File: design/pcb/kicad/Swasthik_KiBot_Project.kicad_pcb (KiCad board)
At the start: 2 copper layers, 30.4 x 14.7 mm, 5 parts, among them J1 Screw_Terminal_01x02, J2 Screw_Terminal_01x02, U1 NCP1117-3.3_SOT223

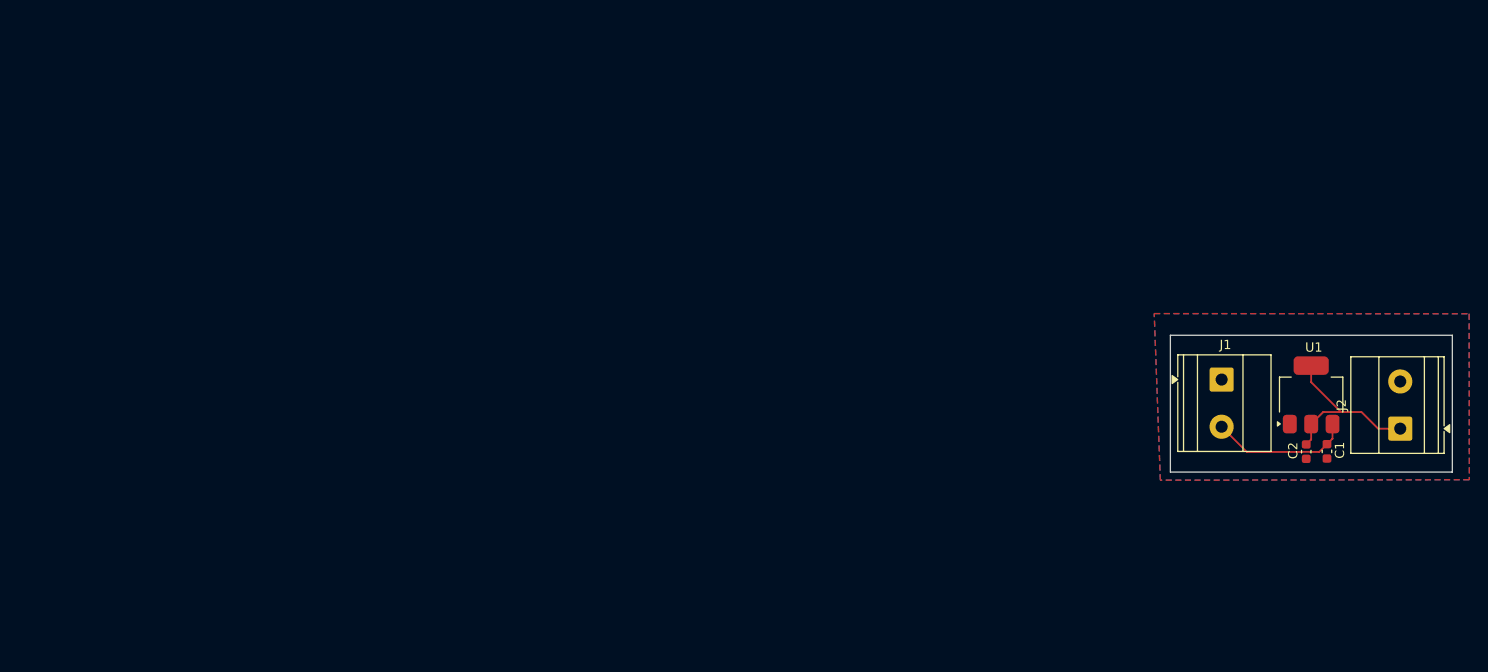
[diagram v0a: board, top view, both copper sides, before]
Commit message: Add LCD and STLink schematic sheets, update KiCad project files
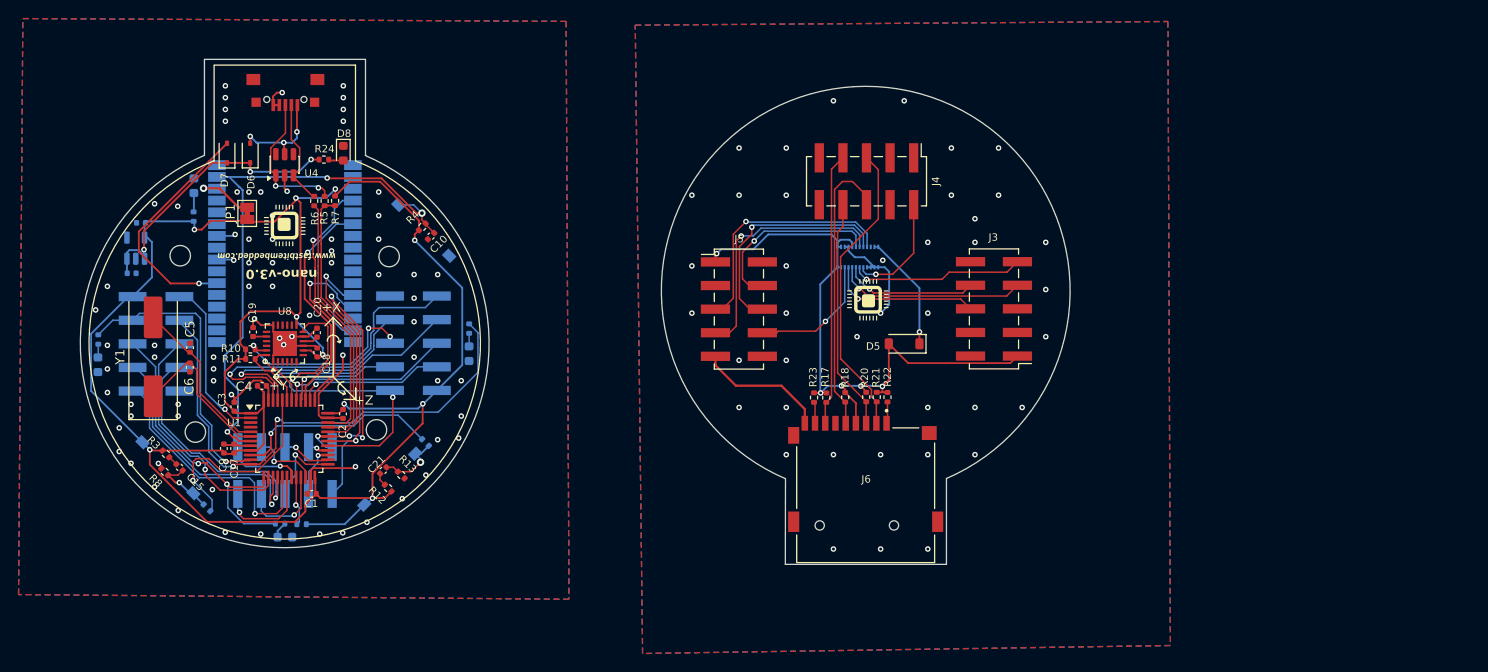
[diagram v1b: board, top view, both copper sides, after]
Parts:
- removed J1: Screw_Terminal_01x02, TerminalBlock_Phoenix:TerminalBlock_Phoenix_MKDS-1,5-2-5.08_1x02_P5.08mm_Horizontal
- added BOOT0: SW3, Button_Switch_SMD:SW_Tactile_SPST_NO_Straight_CK_PTS636Sx25SMTRLFS, B.Cu at (88.5, 80.3)
- added C10: 1uF, Capacitor_SMD:C_0402_1005Metric, F.Cu at (116.8, 55.3)
- added C15: 100nF, Capacitor_SMD:C_0402_1005Metric, F.Cu at (89.7, 80.2)
- added C17: 1uF, Capacitor_SMD:C_0402_1005Metric, F.Cu at (95.6, 78.2)
- added C18: 100nF, Capacitor_SMD:C_0402_1005Metric, F.Cu at (104.5, 67.9)
- added C19: 2.2nF, Capacitor_SMD:C_0402_1005Metric, F.Cu at (97.6, 65.7)
- added C20: 100nF, Capacitor_SMD:C_0402_1005Metric, F.Cu at (104.5, 65.7)
- added C21: 100nF, Capacitor_SMD:C_0402_1005Metric, F.Cu at (111.6, 80.6)
- added C3: 100nF, Capacitor_SMD:C_0402_1005Metric, F.Cu at (95.6, 73.7)
- added C4: 4.7uF, Capacitor_SMD:C_0402_1005Metric, F.Cu at (98.6, 71.5)
- added C5: 20pF, Capacitor_SMD:C_0402_1005Metric, F.Cu at (90.8, 67.3)
- added C6: 20pF, Capacitor_SMD:C_0402_1005Metric, F.Cu at (90.8, 69.5)
- added C7: 1uF, Capacitor_SMD:C_0402_1005Metric, B.Cu at (84.5, 59.3)
- added C8: 1uF, Capacitor_SMD:C_0402_1005Metric, B.Cu at (85.6, 53.9)
- added C9: 10nF, Capacitor_SMD:C_0402_1005Metric, F.Cu at (94.5, 78.2)
- added D1: RED LED, LED_SMD:LED_0603_1608Metric, B.Cu at (91.2, 49.9)
- added D2: BLUE LED, LED_SMD:LED_0603_1608Metric, B.Cu at (80.9, 69.2)
- added D3: GREEN LED, LED_SMD:LED_0603_1608Metric, B.Cu at (120.9, 68.0)
- added D4: RED LED, LED_SMD:LED_0603_1608Metric, B.Cu at (101.0, 87.7)
- added D5: 1N5819WS, Diode_SMD:D_SOD-123, F.Cu at (167.7, 66.9)
- added D6: 1N5819WS, Diode_SMD:D_SOD-323, F.Cu at (97.3, 46.4)
- added D7: 1N5819WS, Diode_SMD:D_SOD-323, F.Cu at (94.8, 46.4)
- added D8: RED LED, LED_SMD:LED_0603_1608Metric, F.Cu at (107.3, 46.4)
- added G***: LOGO, newdemo.preety:nano, F.Cu at (163.8, 62.2)
- added G***: LOGO, newdemo.preety:nano, F.Cu at (101.0, 54.2)
- added G***: LOGO, newdemo.preety:SD_C, B.Cu at (167.7, 88.6)
- added G***: LOGO, newdemo.preety:nano, B.Cu at (101.2, 73.5)
- added H1: MountingHole, MountingHole:MountingHole_2.2mm_M2, B.Cu at (110.9, 76.2)
- added H2: MountingHole, MountingHole:MountingHole_2.2mm_M2, B.Cu at (91.4, 76.4)
- added H3: MountingHole, MountingHole:MountingHole_2.2mm_M2, B.Cu at (112.3, 57.5)
- added H4: MountingHole, MountingHole:MountingHole_2.2mm_M2, B.Cu at (89.8, 57.4)
- added J3: Conn_02x05_Odd_Even, Connector_PinHeader_2.54mm:PinHeader_2x05_P2.54mm_Vertical_SMD, F.Cu at (177.4, 63.2)
- added J4: Conn_02x05_Odd_Even, Connector_PinHeader_2.54mm:PinHeader_2x05_P2.54mm_Vertical_SMD, F.Cu at (163.7, 49.4)
- added J5: Conn_02x05_Odd_Even, Connector_PinHeader_2.54mm:PinHeader_2x05_P2.54mm_Vertical_SMD, F.Cu at (149.9, 63.2)
- added J6: Micro_SD_Card_Det1, fp:CUI_MSD-1-A, F.Cu at (163.6, 83.2)
- added JP1: SolderJumper_2_Open, Jumper:SolderJumper-2_P1.3mm_Bridged_Pad1.0x1.5mm, F.Cu at (97.0, 52.9)
- added P1: Conn_02x05_Odd_Even, Connector_PinSocket_2.54mm:PinSocket_2x05_P2.54mm_Vertical_SMD, B.Cu at (87.2, 66.9)
- added P2: Conn_02x05_Odd_Even, Connector_PinSocket_2.54mm:PinSocket_2x05_P2.54mm_Vertical_SMD, B.Cu at (101.1, 80.6)
- added P3: Conn_02x05_Odd_Even, Connector_PinSocket_2.54mm:PinSocket_2x05_P2.54mm_Vertical_SMD, B.Cu at (114.9, 66.9)
- added R1: 330, Resistor_SMD:R_0402_1005Metric, B.Cu at (91.2, 53.2)
- added R10: 2.2K, Resistor_SMD:R_0402_1005Metric, F.Cu at (97.3, 67.5)
- added R11: 2.2K, Resistor_SMD:R_0402_1005Metric, F.Cu at (97.3, 68.6)
- added R12: 100, Resistor_SMD:R_0402_1005Metric, F.Cu at (112.2, 82.5)
- added R13: 10K, Resistor_SMD:R_0402_1005Metric, F.Cu at (113.6, 81.1)
- added R14: 330, Resistor_SMD:R_0402_1005Metric, B.Cu at (116.2, 77.6)
- added R15: 330, Resistor_SMD:R_0402_1005Metric, B.Cu at (120.9, 65.3)
- added R16: 330, Resistor_SMD:R_0402_1005Metric, B.Cu at (100.5, 86.3)
- added R17: 10K, Resistor_SMD:R_0402_1005Metric, F.Cu at (159.3, 72.7)
- added R18: 10K, Resistor_SMD:R_0402_1005Metric, F.Cu at (161.4, 72.7)
- added R19: 10K, Resistor_SMD:R_0402_1005Metric, B.Cu at (102.8, 86.3)
- added R2: 330, Resistor_SMD:R_0402_1005Metric, B.Cu at (81.0, 66.5)
- added R20: 10K, Resistor_SMD:R_0402_1005Metric, F.Cu at (163.6, 72.7)
- added R21: 10K, Resistor_SMD:R_0402_1005Metric, F.Cu at (164.8, 72.7)
- added R22: 10K, Resistor_SMD:R_0402_1005Metric, F.Cu at (165.9, 72.7)
- added R23: 10K, Resistor_SMD:R_0402_1005Metric, F.Cu at (158.0, 72.7)
- added R24: 330, Resistor_SMD:R_0402_1005Metric, F.Cu at (105.2, 47.1)
- added R3: 100, Resistor_SMD:R_0402_1005Metric, F.Cu at (88.2, 78.8)
- added R4: 10K, Resistor_SMD:R_0402_1005Metric, F.Cu at (115.8, 54.3)
- added R5: 20, Resistor_SMD:R_0402_1005Metric, F.Cu at (105.3, 51.6)
- added R6: 20, Resistor_SMD:R_0402_1005Metric, F.Cu at (104.2, 51.6)
- added R7: 1.5K, Resistor_SMD:R_0402_1005Metric, F.Cu at (106.5, 51.5)
- added R8: 10K, Resistor_SMD:R_0402_1005Metric, F.Cu at (88.1, 80.7)
- added R9: 330, Resistor_SMD:R_0402_1005Metric, B.Cu at (92.7, 84.6)
- added RESET1: SW1, Button_Switch_SMD:SW_Tactile_SPST_NO_Straight_CK_PTS636Sx25SMTRLFS, B.Cu at (116.0, 54.7)
- added U3: ~, FPC_CONNECTOR24:OK-24F024-04, B.Cu at (162.6, 60.2)
- added U4: CDSOT236-0504C, Package_TO_SOT_SMD:SOT-23-6, F.Cu at (101.0, 47.6)
- added U5: TLV75733PDBV, Package_TO_SOT_SMD:SOT-23-5, B.Cu at (85.0, 56.6)
- added U6: STLINK-V3MODS, model:MODULE_STLINK-V3MODS, B.Cu at (101.0, 37.8)
- added U8: MPU6050, Package_DFN_QFN:QFN-24-1EP_4x4mm_P0.5mm_EP2.7x2.6mm, F.Cu at (101.0, 66.9)
- added USER1: SW2, Button_Switch_SMD:SW_Tactile_SPST_NO_Straight_CK_PTS636Sx25SMTRLFS, B.Cu at (112.3, 81.5)
- added Y1: 8MHz Crystal, Crystal:Crystal_SMD_HC49-SD, F.Cu at (86.9, 68.3)
- C1, C2: value 1uF -> 100nF; footprint Capacitor_SMD:C_0603_1608Metric -> Capacitor_SMD:C_0402_1005Metric
- J2: value Screw_Terminal_01x02 -> USB_B_Micro; footprint TerminalBlock_Phoenix:TerminalBlock_Phoenix_MKDS-1,5-2-5.08_1x02_P5.08mm_Horizontal -> FB_Library:micro_USB
- U1: value NCP1117-3.3_SOT223 -> STM32F303CCTx; footprint Package_TO_SOT_SMD:SOT-223-3_TabPin2 -> Package_QFP:LQFP-48_7x7mm_P0.5mm
- moved J2 125.8 mm to (101.1, 38.5), turned to 180 degrees
- moved U1 110.1 mm to (101.5, 77.2), turned to 0 degrees
- moved C1 109.4 mm to (103.9, 83.1), turned to 180 degrees
- moved C2 103.8 mm to (107.3, 74.5)
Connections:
- C1 pad 1: Net-(J1-Pin_2) -> +3V3
- C2 pad 1: Net-(J2-Pin_1) -> +3V3
- J2 pad 1: Net-(J2-Pin_1) -> Net-(D6-A)
- J2 pad 2: GND -> Net-(J2-D-)
- U1 pad 1: GND -> +3V3
- U1 pad 2: Net-(J2-Pin_1) -> PC13
- U1 pad 3: Net-(J1-Pin_2) -> unconnected-(U1-PC14-Pad3)
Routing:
- net +3V3: track 0.00 -> 220.2 mm, vias 0 -> 10
- net +3.3V: track 0.00 -> 71.5 mm, vias 0 -> 5
- net RESET: track 0.00 -> 63.4 mm, vias 0 -> 3
- net LED_2: track 0.00 -> 56.9 mm, vias 0 -> 2
- net GND: track 0.00 -> 55.6 mm, vias 0 -> 77
- net MPU_INT: track 0.00 -> 35.8 mm, vias 0 -> 2
- net PB9: track 0.00 -> 34.9 mm, vias 0 -> 1
- net LED_3: track 0.00 -> 33.7 mm, vias 0 -> 2
- net USART1_TX: track 0.00 -> 33.5 mm, vias 0 -> 2
- net SD_CS: track 0.00 -> 32.5 mm
- net LED_1: track 0.00 -> 31.8 mm, vias 0 -> 1
- net +5V: track 0.00 -> 31.2 mm, vias 0 -> 3
- net SD_SCL: track 0.00 -> 31.1 mm
- net SWDIO: track 0.00 -> 30.4 mm, vias 0 -> 1
- net USB_DP: track 0.00 -> 29.6 mm
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- added copper zone on B.Cu, net GND1
- added copper zone on F.Cu, net GND1
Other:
- board size 30.4 x 14.7 mm -> 106.6 x 54.4 mm
- board text added: "+X"
- board text added: "+Y"
- board text added: "+Z"
- board text added: "FASTBIT EMBEDDED"
- board text added: "Nano LCD Shield"
- board text added: "nano-v3.0"
- board text added: "www.fastbitembedded.com"
- board text added: "µSD Card"
